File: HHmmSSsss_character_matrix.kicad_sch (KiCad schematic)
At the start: 39 parts, among them U24 10016AS, U25 10016AS, U26 SN74LVC244A, U27 10016AS, U28 10016AS, U29 10016AS, U30 10016AS, U31 SN74LVC244A, U32 10016AS, U33 10016AS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

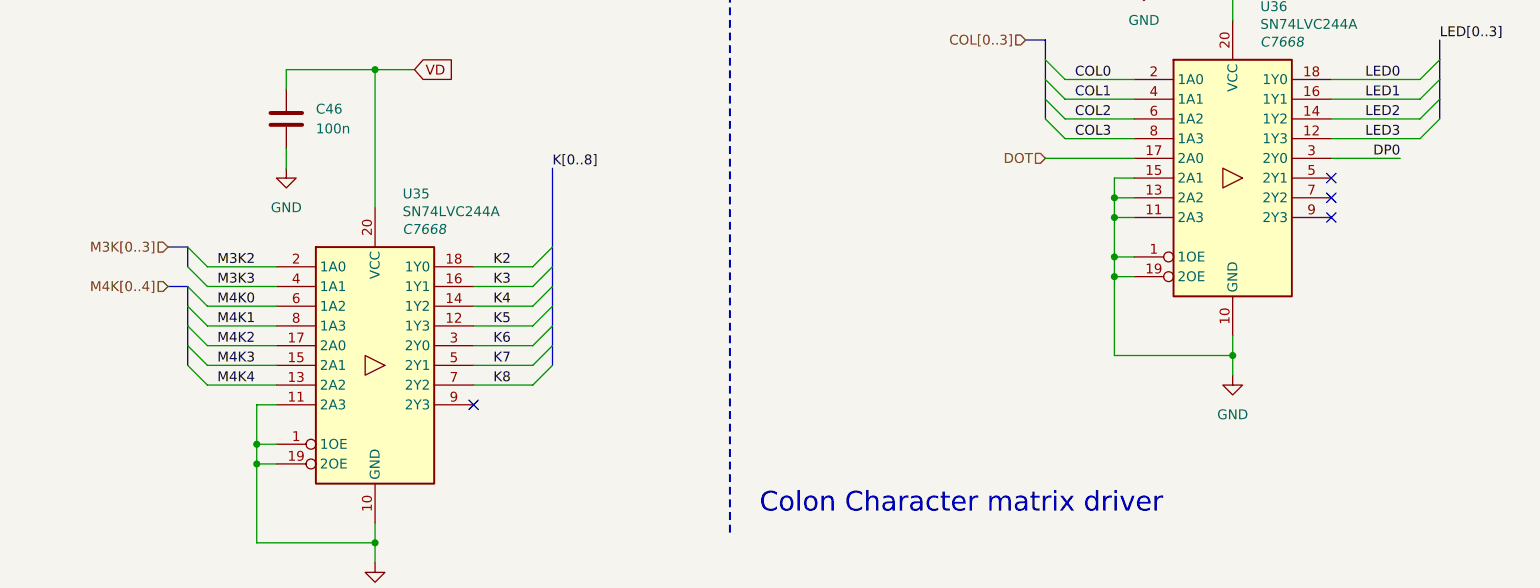
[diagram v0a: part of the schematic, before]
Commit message: Power stage changes
- removal of potentiometer
- addition of rotary encoder
- addition of ambient light sensor
- addition of unity gain differential amplifier.
- reording of the schematic.
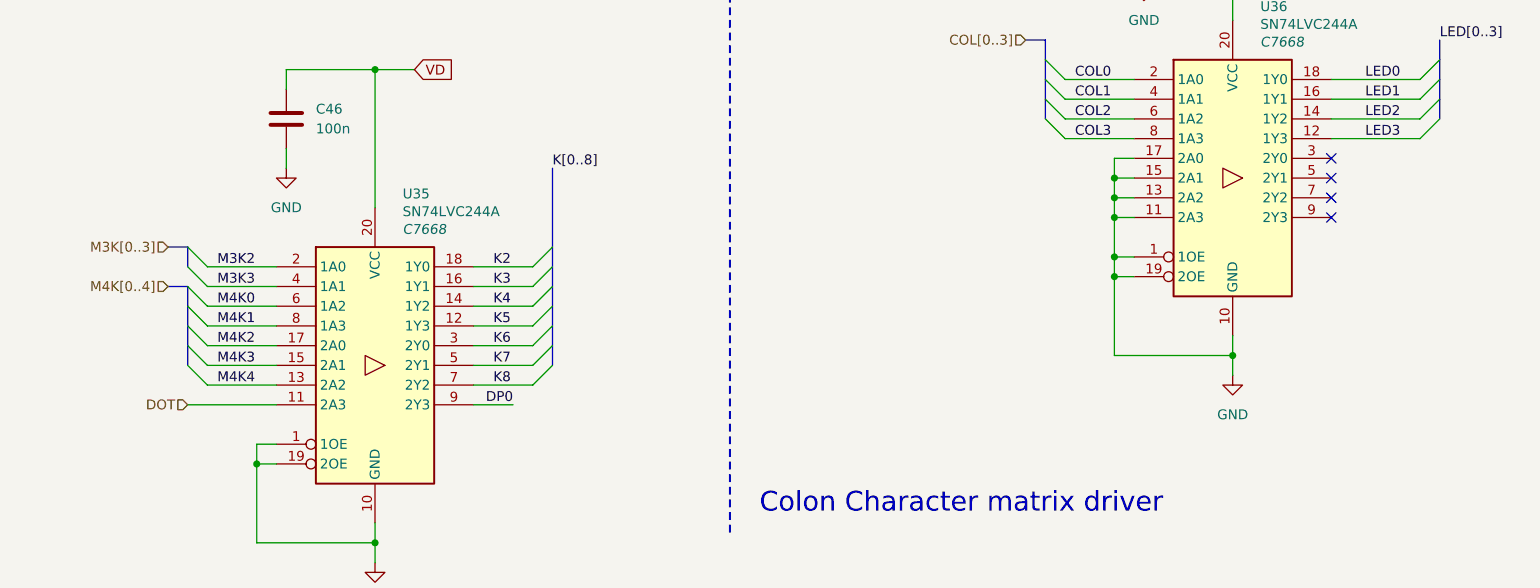
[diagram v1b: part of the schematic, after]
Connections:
- net DOT: now also U35.11 (2A3); no longer U36.17 (2A0)
- net DP0: now also U35.9 (2Y3); no longer U36.3 (2Y0)
- net GND: now also U36.17 (2A0); no longer U35.11 (2A3)
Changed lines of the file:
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@@
 	)
 	(junction
-		(at 238.76 241.3)
-		(diameter 0)
-		(color 0 0 0 0)
-	)
-	(junction
 		(at 370.84 100.33)
 		(diameter 0)
@@
 	)
 	(junction
-		(at 137.16 243.84)
+		(at 349.25 207.01)
 		(diameter 0)
 		(color 0 0 0 0)
 	)
-	(no_connect
-		(at 266.7 236.22)
+	(junction
+		(at 137.16 243.84)
+		(diameter 0)
+		(color 0 0 0 0)
 	)
 	(no_connect
@@
 	)
 	(no_connect
+		(at 377.19 204.47)
+	)
+	(no_connect
 		(at 69.85 146.05)
 	)
@@
 	(wire
 		(pts
+			(xy 229.87 236.22) (xy 241.3 236.22)
+		)
+		(stroke
+			(width 0)
+			(type default)
+		)
+	)
+	(wire
+		(pts
 			(xy 128.27 143.51) (xy 133.35 143.51)
 		)
@@
 	(wire
 		(pts
-			(xy 238.76 236.22) (xy 241.3 236.22)
-		)
-		(stroke
-			(width 0)
-			(type default)
-		)
-	)
-	(wire
-		(pts
 			(xy 39.37 233.68) (xy 48.26 233.68)
 		)
@@
 		)
 	)
+	(wire
+		(pts
+			(xy 349.25 204.47) (xy 351.79 204.47)
+		)
+		(stroke
+			(width 0)
+			(type default)
+		)
+	)
 	(bus
 		(pts
@@
 		)
 	)
+	(wire
+		(pts
+			(xy 266.7 236.22) (xy 271.78 236.22)
+		)
+		(stroke
+			(width 0)
+			(type default)
+		)
+	)
 	(bus
 		(pts
@@
 	(wire
 		(pts
+			(xy 349.25 207.01) (xy 349.25 204.47)
+		)
+		(stroke
+			(width 0)
+			(type default)
+		)
+	)
+	(wire
+		(pts
 			(xy 128.27 54.61) (xy 133.35 54.61)
 		)
@@
 	(wire
 		(pts
-			(xy 377.19 204.47) (xy 386.08 204.47)
-		)
-		(stroke
-			(width 0)
-			(type default)
-		)
-	)
-	(wire
-		(pts
 			(xy 39.37 228.6) (xy 48.26 228.6)
 		)
@@
 	(wire
 		(pts
-			(xy 340.36 204.47) (xy 351.79 204.47)
-		)
-		(stroke
-			(width 0)
-			(type default)
-		)
-	)
-	(wire
-		(pts
 			(xy 349.25 212.09) (xy 349.25 209.55)
 		)
@@
 	(wire
 		(pts
-			(xy 238.76 241.3) (xy 238.76 236.22)
-		)
-		(stroke
-			(width 0)
-			(type default)
-		)
-	)
-	(wire
-		(pts
 			(xy 353.06 168.91) (xy 364.49 168.91)
 		)
@@
 		)
 	)
-	(label "DP0"
-		(at 386.08 204.47 180)
-		(effects
-			(font
-				(size 1.27 1.27)
-			)
-			(justify right bottom)
-		)
-	)
 	(label "A4"
 		(at 128.27 59.69 0)
@@
 		)
 	)
+	(label "DP0"
+		(at 271.78 236.22 180)
+		(effects
+			(font
+				(size 1.27 1.27)
+			)
+			(justify right bottom)
+		)
+	)
 	(label "A6"
 		(at 175.26 64.77 0)
@@
 	(hierarchical_label "DOT"
 		(shape input)
-		(at 340.36 204.47 180)
+		(at 229.87 236.22 180)
 		(effects
 			(font
